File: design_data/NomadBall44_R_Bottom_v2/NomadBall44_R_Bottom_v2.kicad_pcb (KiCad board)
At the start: 2 copper layers, 147.4 x 96.5 mm, 57 parts, among them SW1 SW_Push, SW10 SW_Push, SW11 SW_Push, SW12 SW_Push, SW13 SW_Push, SW14 SW_Push, SW15 SW_Push, SW16 SW_Push, SW17 SW_Push, SW18 SW_Push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

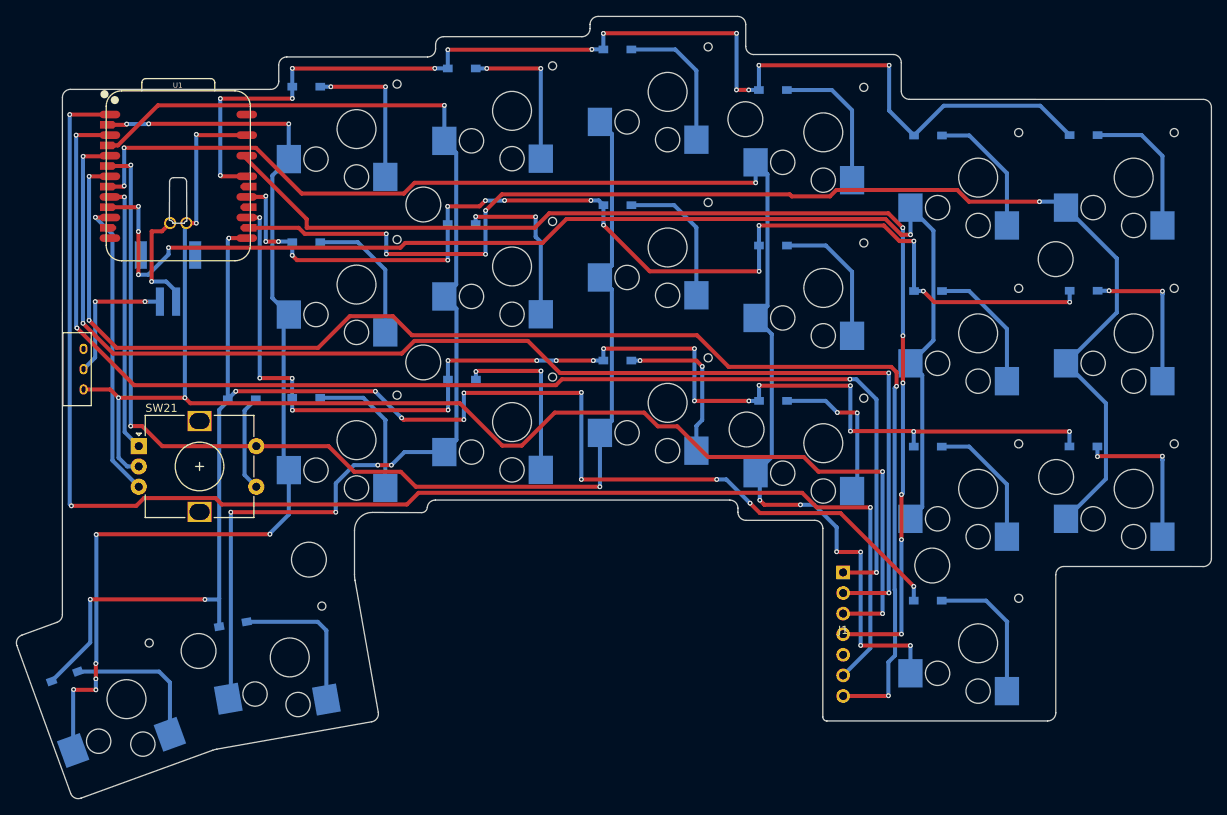
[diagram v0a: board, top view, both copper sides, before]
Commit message: キースイッチとダイオードを削除
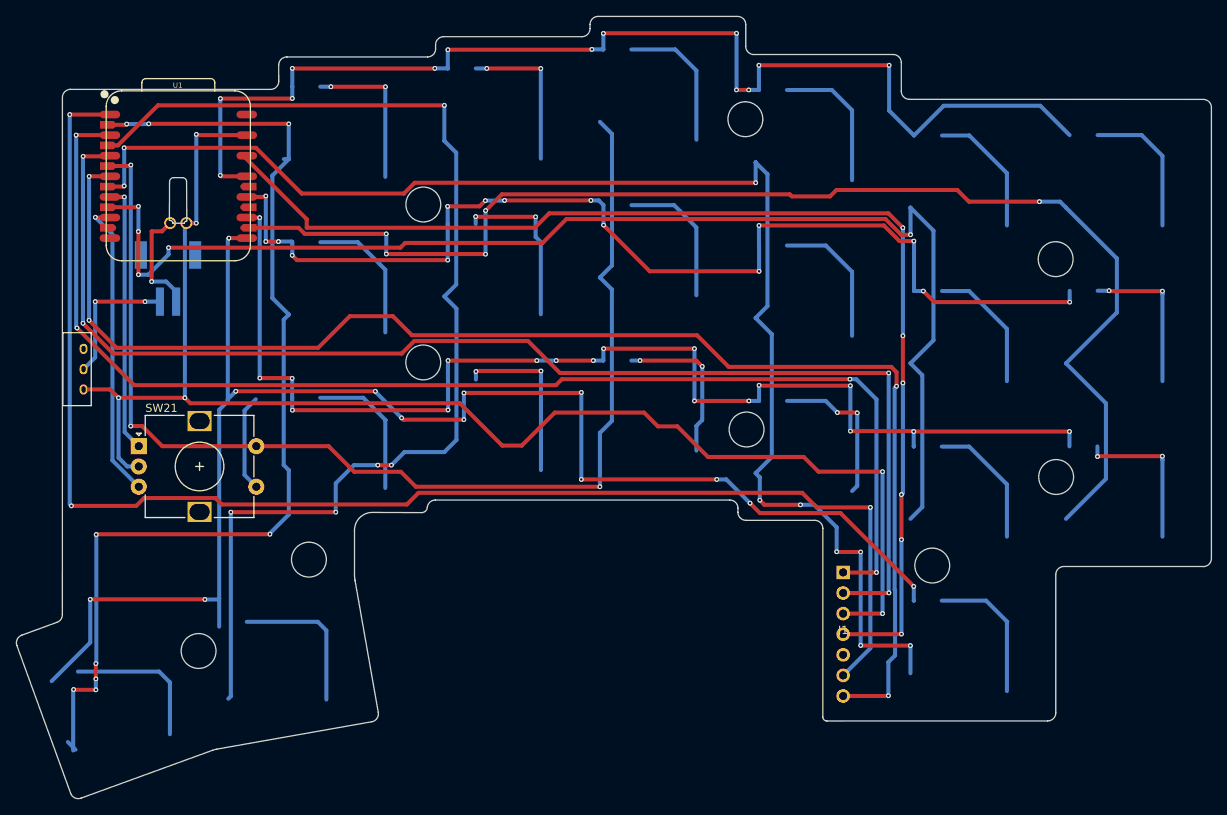
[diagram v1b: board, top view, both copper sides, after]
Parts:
- removed D1, D10, D11, D12, D13, D14, D15, D16, D17, D18, D19, D2, D20, D21, D22, D3, D4, D5, D6, D7, D8, D9: D, NomadBall44:Diode_SMD
- removed SW1, SW10, SW11, SW12, SW13, SW14, SW15, SW16, SW17, SW18, SW19, SW2, SW20, SW22, SW3, SW4, SW5, SW6, SW7, SW8, SW9: SW_Push, NomadBall44:Choc_v2_Hotswap_1u

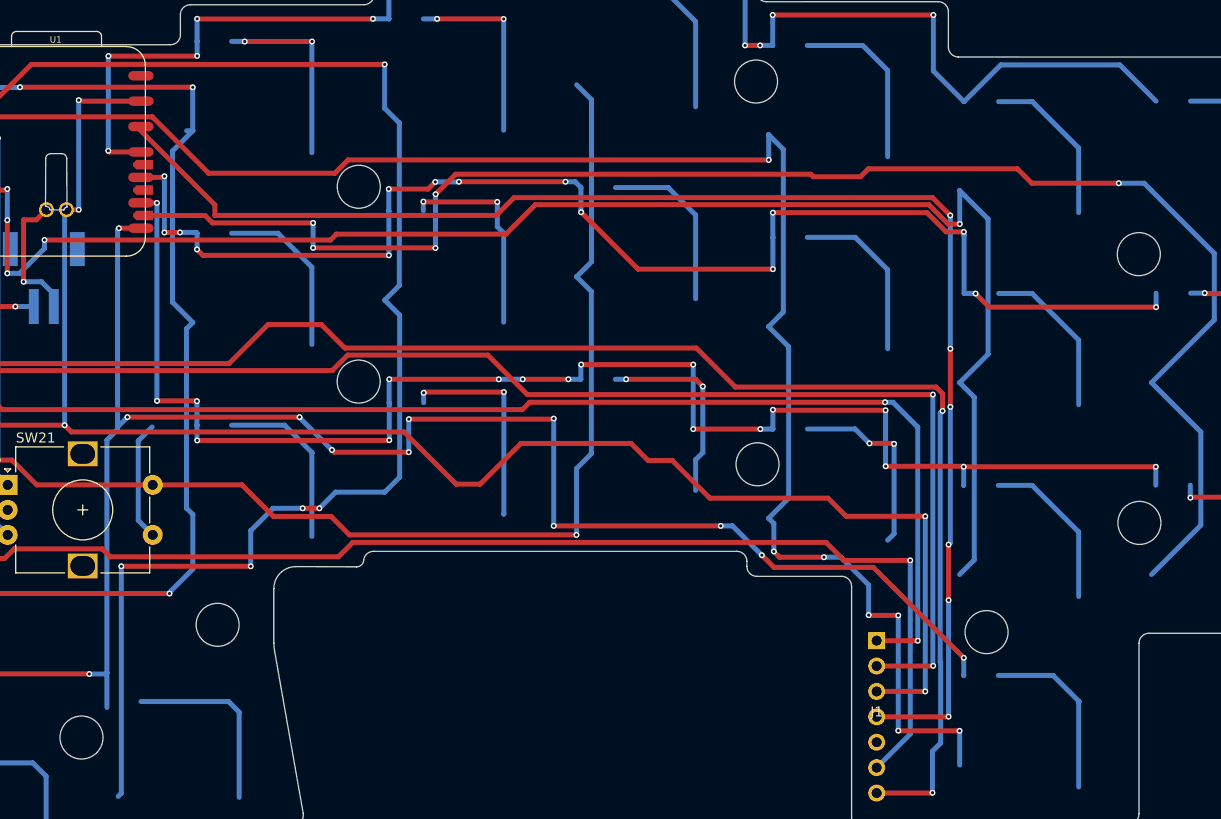
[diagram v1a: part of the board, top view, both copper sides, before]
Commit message: ネジ穴を追加
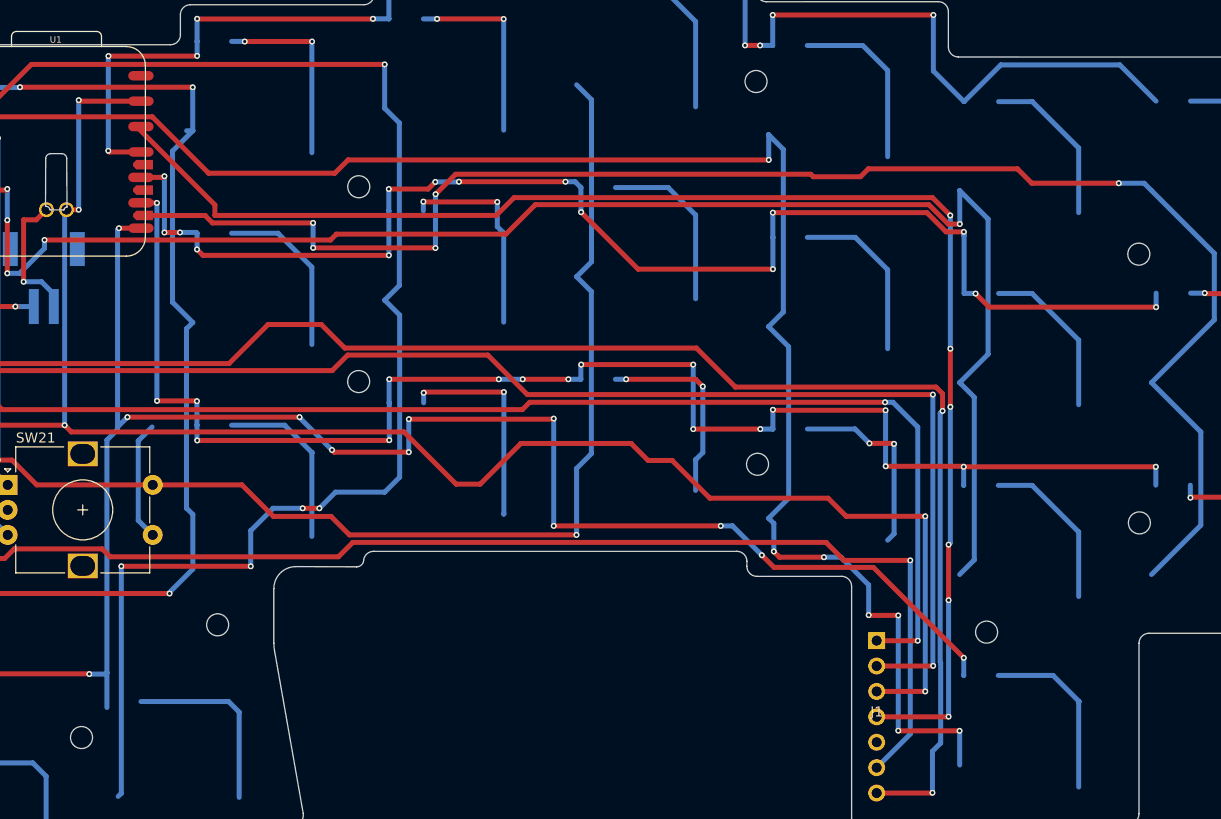
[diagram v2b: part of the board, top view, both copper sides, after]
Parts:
- REF** (x9): value MountingHole_4.3mm_M4 -> Val**; footprint MountingHole:MountingHole_4.3mm_M4 -> NomadBall44:m2_Screw_Hole_EdgeCuts

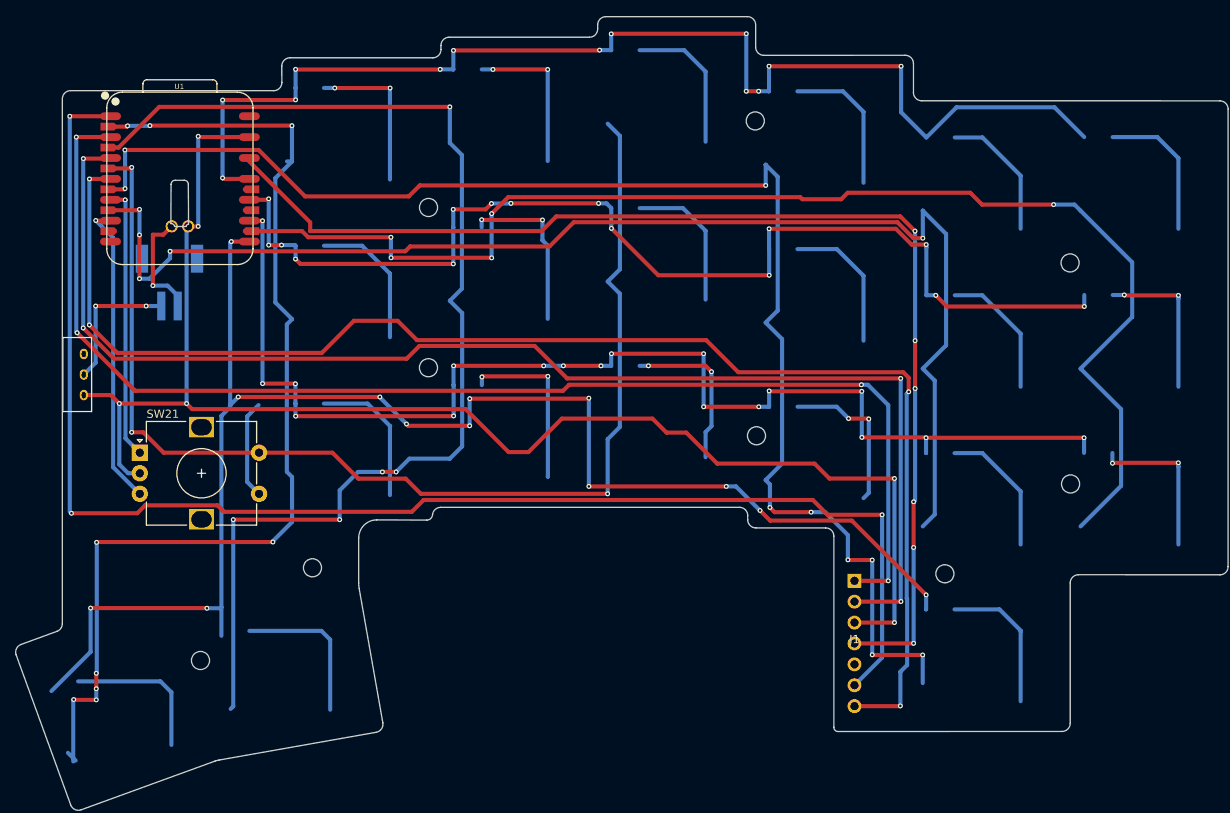
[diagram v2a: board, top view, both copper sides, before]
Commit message: 配線を削除
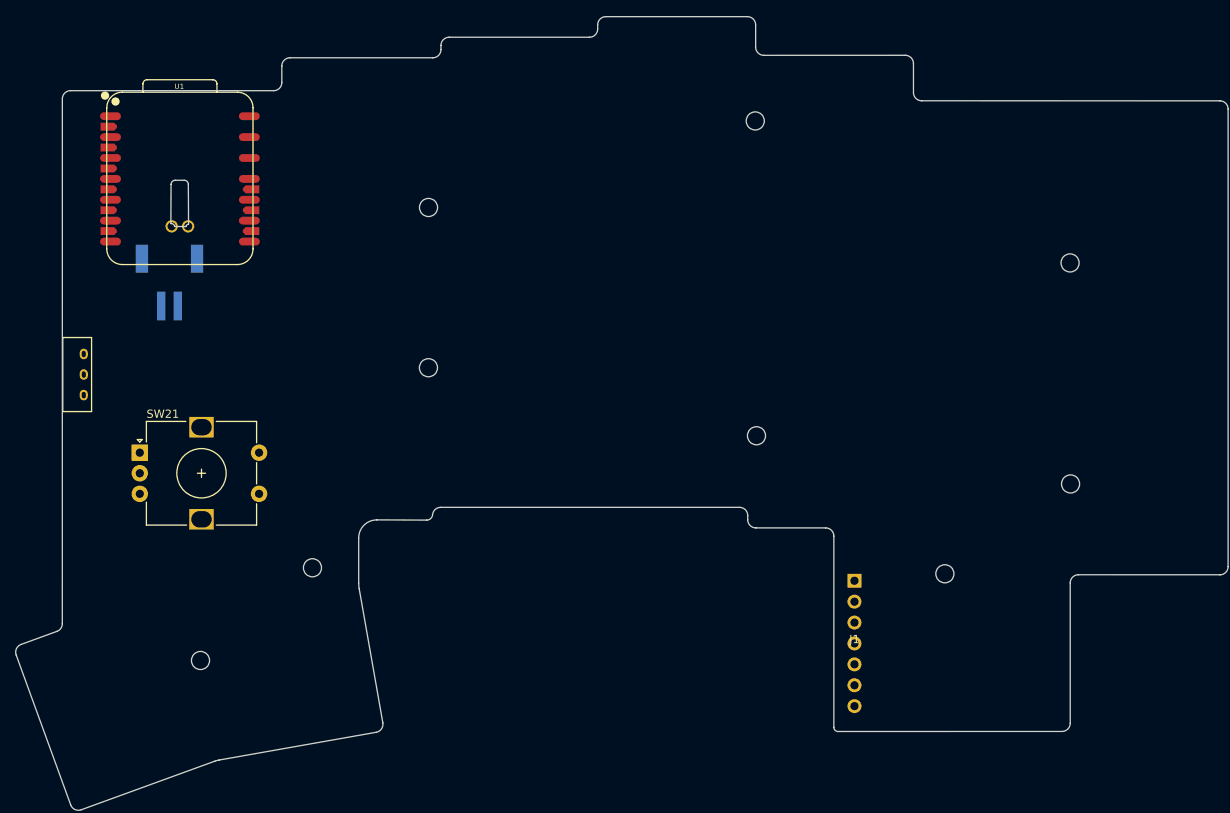
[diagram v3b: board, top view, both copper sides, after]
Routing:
- net Row3: track 185.6 -> 0.00 mm, vias 13 -> 0
- net GND: track 177.7 -> 0.03 mm, vias 6 -> 0
- net SDIO: track 176.8 -> 0.01 mm, vias 3 -> 0
- net Col3: track 172.8 -> 0.00 mm, vias 9 -> 0
- net MOTION: track 172.6 -> 0.01 mm, vias 4 -> 0
- net CS: track 160.7 -> 0.11 mm, vias 4 -> 0
- net Col5: track 158.8 -> 0.00 mm, vias 5 -> 0
- net SCLK: track 157.1 -> 0.02 mm, vias 4 -> 0
- net Col4: track 156.9 -> 0.00 mm, vias 5 -> 0
- net Row2: track 151.3 -> 0.02 mm, vias 18 -> 0
- net Row0: track 144.7 -> 0.00 mm, vias 13 -> 0
- net 3.3V: track 144.9 -> 0.37 mm, vias 6 -> 0
- net Col2: track 143.5 -> 0.00 mm, vias 3 -> 0
- net Col1: track 143.4 -> 0.00 mm, vias 5 -> 0
- net Row1: track 136.5 -> 0.00 mm, vias 15 -> 0
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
